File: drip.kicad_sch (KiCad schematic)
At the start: 81 parts, among them J1 ISP, J2 2xAA Battery Holder, Q1 2n2907, Q2 2n2907, Q3 2n2907, Q4 2n2907, Q5 2n2907, Q6 2n2907, Q7 2n2907, Q8 2n2907, Q9 2n2222, SW1 Bin, SW10 Recall, SW11 D, SW12 A, SW13 7, SW14 4, SW15 1, SW16 0, SW17 Hex, SW18 E, SW19 B, SW2 Store, SW20 8, SW21 5, SW22 2, SW23 Decimal, SW24 Oct, SW25 F, SW26 C, SW27 9, SW28 6, SW29 3, SW3 Shift, SW30 +/-, SW31 Clear, SW32 K, SW33 Div, SW34 Mul, SW35 Minus, SW36 Plus, SW37 Enter, SW4 1'sCompl, SW5 Or, SW6 And, SW7 Xor, SW8 Clear Entry, SW9 Dec, U1 74HC138, U2 5641AS-4Digit-7Segment, U3 5641AS-4Digit-7Segment, U4 MSP430G2553IN20, U5 74HC251, U6 74HC138, U7 74HC595

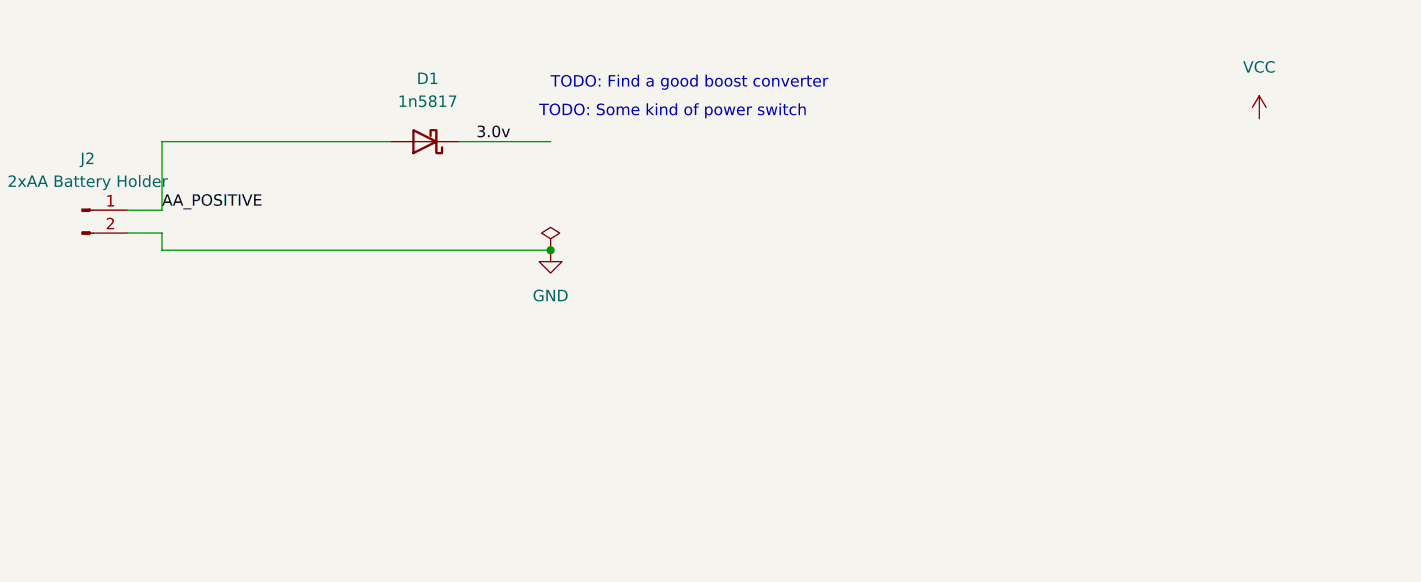
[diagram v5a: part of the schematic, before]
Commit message: Step-up converter, layout of keypad
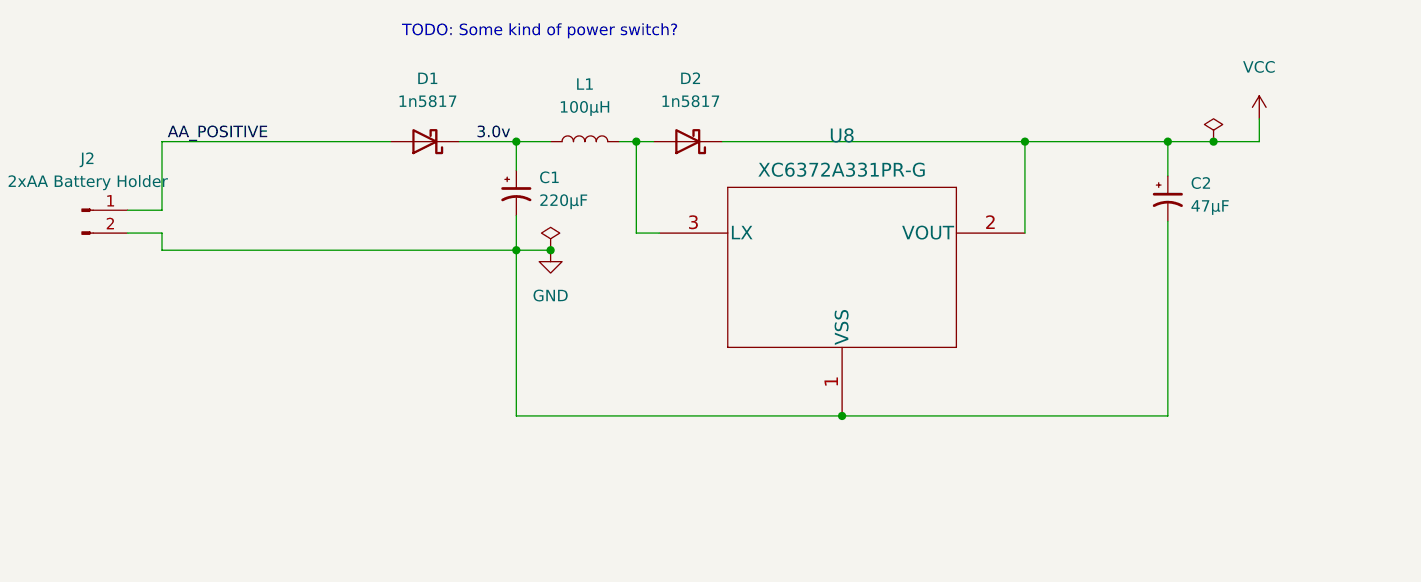
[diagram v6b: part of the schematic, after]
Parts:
- added C1: 220µF, Capacitor_THT:CP_Radial_D8.0mm_P5.00mm, symbol Device:C_Polarized_Small_US
- added C2: 47µF, Capacitor_Tantalum_SMD:CP_EIA-3528-15_AVX-H_Pad1.50x2.35mm_HandSolder, symbol Device:C_Polarized_Small_US
- added D2: 1n5817, Diode_THT:D_DO-41_SOD81_P10.16mm_Horizontal, symbol Device:D_Schottky
- added L1: 100µH, Inductor_SMD:L_0805_2012Metric_Pad1.15x1.40mm_HandSolder, symbol Device:L
- added U8: XC6372A331PR-G, Package_TO_SOT_SMD:SOT-89-3_Handsoldering, symbol XC6372A331PR:XC6372A331PR-G
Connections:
- net 3.0v: now also C1.1, L1.1
- net GND: now also C1.2, C2.2, U8.1 (VSS)
- net VCC: now also C2.1, D2.1 (K), U8.2 (VOUT)
- new net: D2.2 (A), L1.2, U8.3 (LX)
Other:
- note added: "TODO: Some kind of power switch?"
- note removed: "TODO: Find a good boost converter"
- note removed: "TODO: Some kind of power switch"

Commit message: Test hooks
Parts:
- added TP1: 3.3v, TestPoint:TestPoint_Loop_D2.50mm_Drill1.85mm, symbol Connector:TestPoint
- added TP2: GND, TestPoint:TestPoint_Loop_D2.50mm_Drill1.85mm, symbol Connector:TestPoint
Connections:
- net GND: now also TP2.1
- net VCC: now also TP1.1
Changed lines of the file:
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@@
+    (stroke (width 0) (type default) (color 0 0 0 0))
+  )
+  (wire (pts (xy 318.77 296.545) (xy 323.215 296.545))
     (stroke (width 0) (type default) (color 0 0 0 0))
   )
@@
     (pin "1")
     (pin "2")
+  )
+  (symbol (lib_id "Connector:TestPoint") (at 334.01 296.545 0) (unit 1)
+    (in_bom yes) (on_board yes) (fields_autoplaced)
+    (property "Reference" "TP2" (id 0) (at 336.55 291.9729 0)
+      (effects (font (size 1.27 1.27)) (justify left))
+    )
+    (property "Value" "GND" (id 1) (at 336.55 294.5129 0)
+      (effects (font (size 1.27 1.27)) (justify left))
+    )
+    (property "Footprint" "TestPoint:TestPoint_Loop_D2.50mm_Drill1.85mm" (id 2) (at 339.09 296.545 0)
+      (effects (font (size 1.27 1.27)) hide)
+    )
+    (property "Datasheet" "~" (id 3) (at 339.09 296.545 0)
+      (effects (font (size 1.27 1.27)) hide)
+    )
+    (pin "1")
   )
   (symbol (lib_id "Switch:SW_Push_45deg") (at 86.995 386.715 0) (unit 1)
@@
     (pin "2")
   )
+  (symbol (lib_id "power:GND") (at 334.01 296.545 0) (unit 1)
+    (in_bom yes) (on_board yes) (fields_autoplaced)
+    (property "Reference" "#PWR04" (id 0) (at 334.01 302.895 0)
+      (effects (font (size 1.27 1.27)) hide)
+    )
+    (property "Value" "GND" (id 1) (at 334.01 300.99 0))
+    (property "Footprint" "" (id 2) (at 334.01 296.545 0)
+      (effects (font (size 1.27 1.27)) hide)
+    )
+    (property "Datasheet" "" (id 3) (at 334.01 296.545 0)
+      (effects (font (size 1.27 1.27)) hide)
+    )
+    (pin "1")
+  )
   (symbol (lib_id "Connector:Conn_01x02_Male") (at 55.88 69.85 0) (unit 1)
     (in_bom yes) (on_board yes) (fields_autoplaced)
@@
     (pin "1")
   )
+  (symbol (lib_id "Connector:TestPoint") (at 323.215 296.545 0) (unit 1)
+    (in_bom yes) (on_board yes) (fields_autoplaced)
+    (property "Reference" "TP1" (id 0) (at 325.12 291.9729 0)
+      (effects (font (size 1.27 1.27)) (justify left))
+    )
+    (property "Value" "3.3v" (id 1) (at 325.12 294.5129 0)
+      (effects (font (size 1.27 1.27)) (justify left))
+    )
+    (property "Footprint" "TestPoint:TestPoint_Loop_D2.50mm_Drill1.85mm" (id 2) (at 328.295 296.545 0)
+      (effects (font (size 1.27 1.27)) hide)
+    )
+    (property "Datasheet" "~" (id 3) (at 328.295 296.545 0)
+      (effects (font (size 1.27 1.27)) hide)
+    )
+    (pin "1")
+  )
   (symbol (lib_id "Switch:SW_Push_45deg") (at 78.74 323.215 0) (unit 1)
     (in_bom yes) (on_board yes) (fields_autoplaced)
@@
     (pin "2")
   )
+  (symbol (lib_id "power:VCC") (at 318.77 296.545 0) (unit 1)
+    (in_bom yes) (on_board yes) (fields_autoplaced)
+    (property "Reference" "#PWR03" (id 0) (at 318.77 300.355 0)
+      (effects (font (size 1.27 1.27)) hide)
+    )
+    (property "Value" "VCC" (id 1) (at 318.77 290.83 0))
+    (property "Footprint" "" (id 2) (at 318.77 296.545 0)
+      (effects (font (size 1.27 1.27)) hide)
+    )
+    (property "Datasheet" "" (id 3) (at 318.77 296.545 0)
+      (effects (font (size 1.27 1.27)) hide)
+    )
+    (pin "1")
+  )
   (symbol (lib_id "Switch:SW_Push_45deg") (at 104.14 361.315 0) (unit 1)
     (in_bom yes) (on_board yes)
@@
       (reference "#PWR02") (unit 1) (value "GND") (footprint "")
     )
+    (path "/b8fe36f4-c454-4599-aba6-20ebd4149fa0"
+      (reference "#PWR03") (unit 1) (value "VCC") (footprint "")
+    )
+    (path "/619df7b3-360d-4fc7-ab2a-c036de3b0705"
+      (reference "#PWR04") (unit 1) (value "GND") (footprint "")
+    )
     (path "/2f993b5f-17bc-43df-9685-e7a00e227a17"
       (reference "#PWR0101") (unit 1) (value "GND") (footprint "")
@@
       (reference "SW37") (unit 1) (value "Enter") (footprint "DripButtons:8mm_G77_Push")
     )
+    (path "/7aef263e-8f79-4d82-8858-7808883e8335"
+      (reference "TP1") (unit 1) (value "3.3v") (footprint "TestPoint:TestPoint_Loop_D2.50mm_Drill1.85mm")
+    )
+    (path "/27a66150-b8ad-4e9b-a26c-00b78d0b1d2a"
+      (reference "TP2") (unit 1) (value "GND") (footprint "TestPoint:TestPoint_Loop_D2.50mm_Drill1.85mm")
+    )
     (path "/1c7d349c-d2da-4ef6-a8a5-45ed3856b2b6"

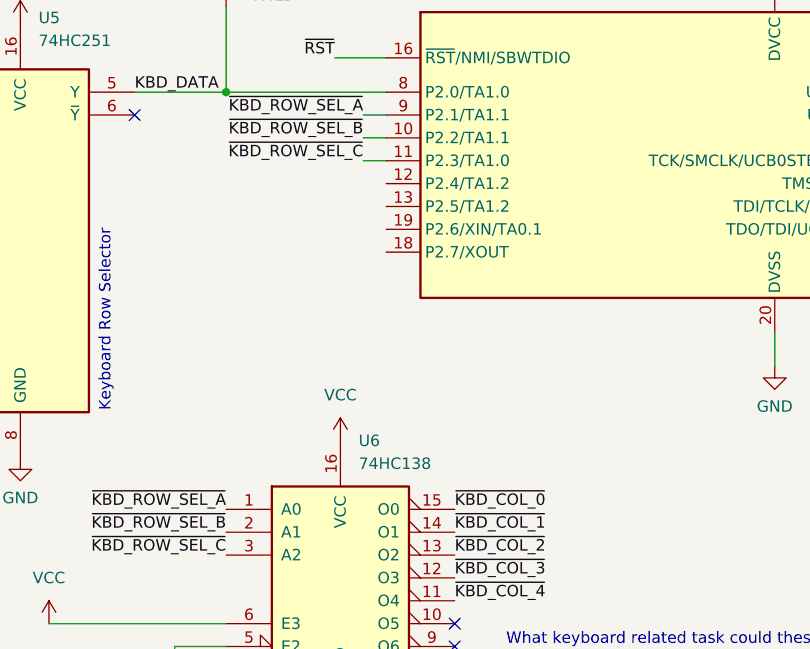
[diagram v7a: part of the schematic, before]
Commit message: Mode LEDs
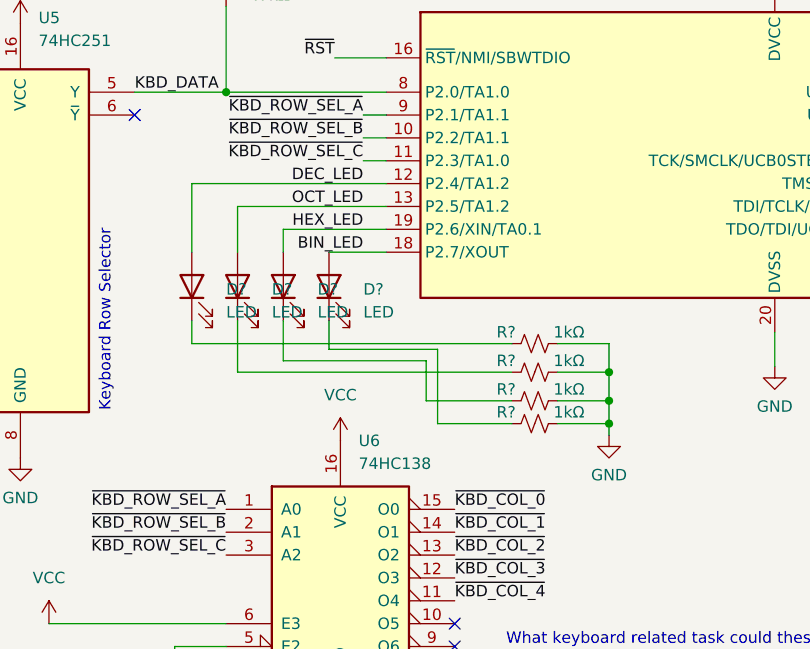
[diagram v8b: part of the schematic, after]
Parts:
- added D? (x4): LED, LED_SMD:LED_0805_2012Metric_Pad1.15x1.40mm_HandSolder, symbol Device:LED
- added R? (x4): 1kΩ, Resistor_SMD:R_0805_2012Metric_Pad1.20x1.40mm_HandSolder, symbol Device:R_Small_US
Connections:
- net GND: now also R?.2, R?.2, R?.2, R?.2
- net DEC_LED: now reaches U4.12 (P2.4/TA1.2)
- net DEC_LED: now also D?.2 (A)
- net OCT_LED: now reaches U4.13 (P2.5/TA1.2)
- net OCT_LED: now also D?.2 (A)
- net BIN_LED: now reaches U4.18 (P2.7/XOUT)
- net BIN_LED: now also D?.2 (A)
- net HEX_LED: now reaches U4.19 (P2.6/XIN/TA0.1)
- net HEX_LED: now also D?.2 (A)
- new net: D?.1 (K), R?.1 (x4)
